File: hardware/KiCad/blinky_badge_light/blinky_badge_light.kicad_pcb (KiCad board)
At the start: 4 copper layers, 108.6 x 87.7 mm, 123 parts, among them Q1 N-Channel MOSFET, Q2 Q_PMOS_GSD, Q3 N-Channel MOSFET, Q4 Q_PMOS_GSD, SW1 TS-1187A-B-A-B, U1 ESP32-S3-WROOM-1, U2 TP4056, U3 AP2112K-3.3, U4 MT3608, U5 CP2102N-Axx-xQFN24, U6 SN74LVC1T45DBV

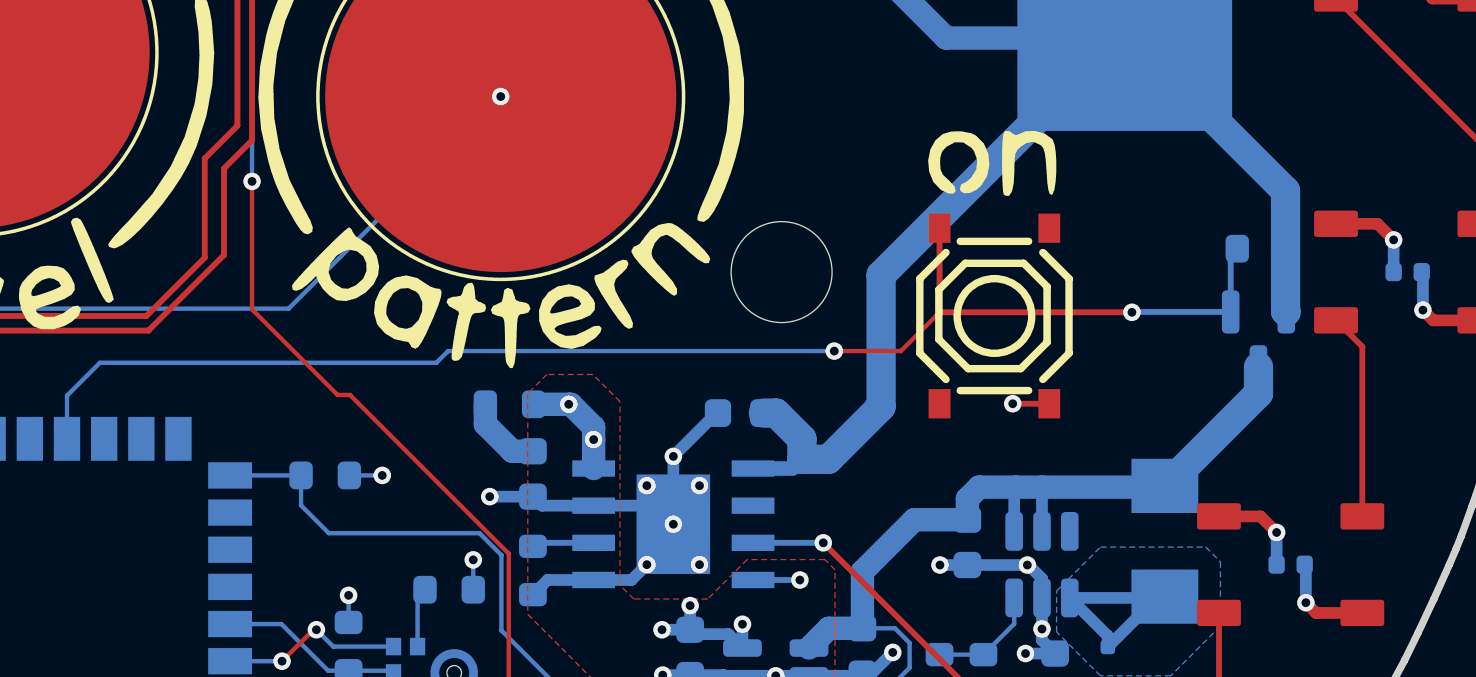
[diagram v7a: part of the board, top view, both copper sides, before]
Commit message: here's an idea.. use schottkey diode so we can detect presses after it's turned on?
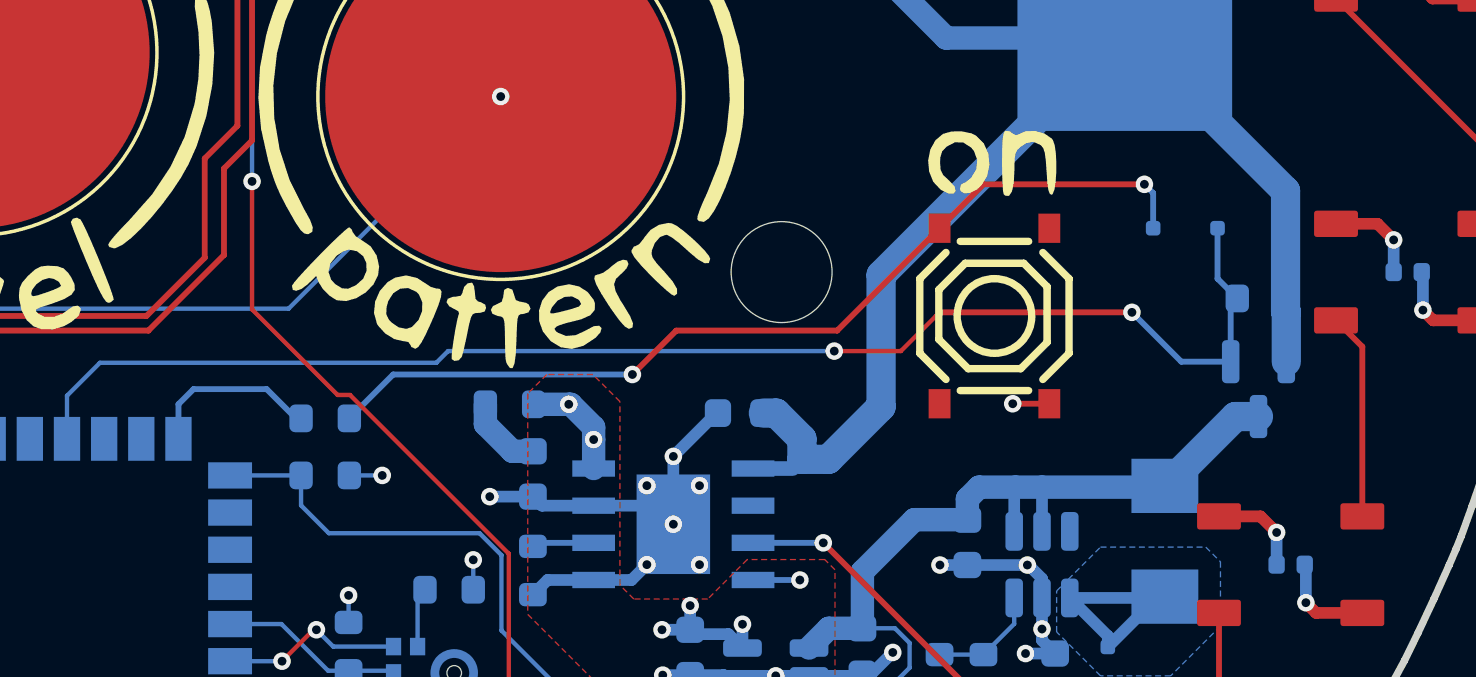
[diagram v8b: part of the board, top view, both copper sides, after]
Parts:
- added D29: D_Schottky, Diode_SMD:D_SOD-323F, B.Cu at (191.4, 87.5)
- added R21: 100kΩ, Resistor_SMD:R_0603_1608Metric, B.Cu at (162.0, 94.0)
- moved Q2 1.70 mm to (193.9, 93.0)
- moved R9 1.70 mm to (194.0, 89.9)
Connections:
- SW1 pad 3: ESP32 Power Control -> Net-(D29-K)
- U1 pad 26: unconnected-(U1-GPIO45-Pad26) -> POWER SENSE
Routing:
- net Net-(D29-K): track 0.00 -> 31.7 mm, vias 0 -> 2
- net POWER SENSE: track 0.00 -> 6.00 mm
- net BAT+: track 137.0 -> 138.7 mm
- net SYSTEM POWER: track 31.1 -> 29.9 mm
- net ESP32 Power Control: track 47.3 -> 48.1 mm
